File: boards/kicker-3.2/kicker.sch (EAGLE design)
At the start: 155 parts, among them J1 B2PS-VH(LF)(SN), J2 HFW8R-1ST, J3 B2PS-VH(LF)(SN), J4 B2PS-VH(LF)(SN), J5 2-PIN_2MM-H, J6 3-PIN_2MM-H, J7 !BTN_KCK_PRE_EXT, J8 !BTN_CHP_PRE_EXT, J9 !BTN_CHG_PRE_EXT, Q1 ATP302ATPAK, Q10 BSS806NSOT-23-3, Q2 IRFS4227, Q3 BSS127, Q4 BSS127, Q5 BSS127, Q6 BSS127, Q7 AOD1N60, T1 DA203X-ALDA2034, U1 MPM3620GQV-P, U2 15V, U3 LT3751FE, U4 AT32ATQFP44, U5 IX4427N, U6 MAX6817, U7 MAX6817

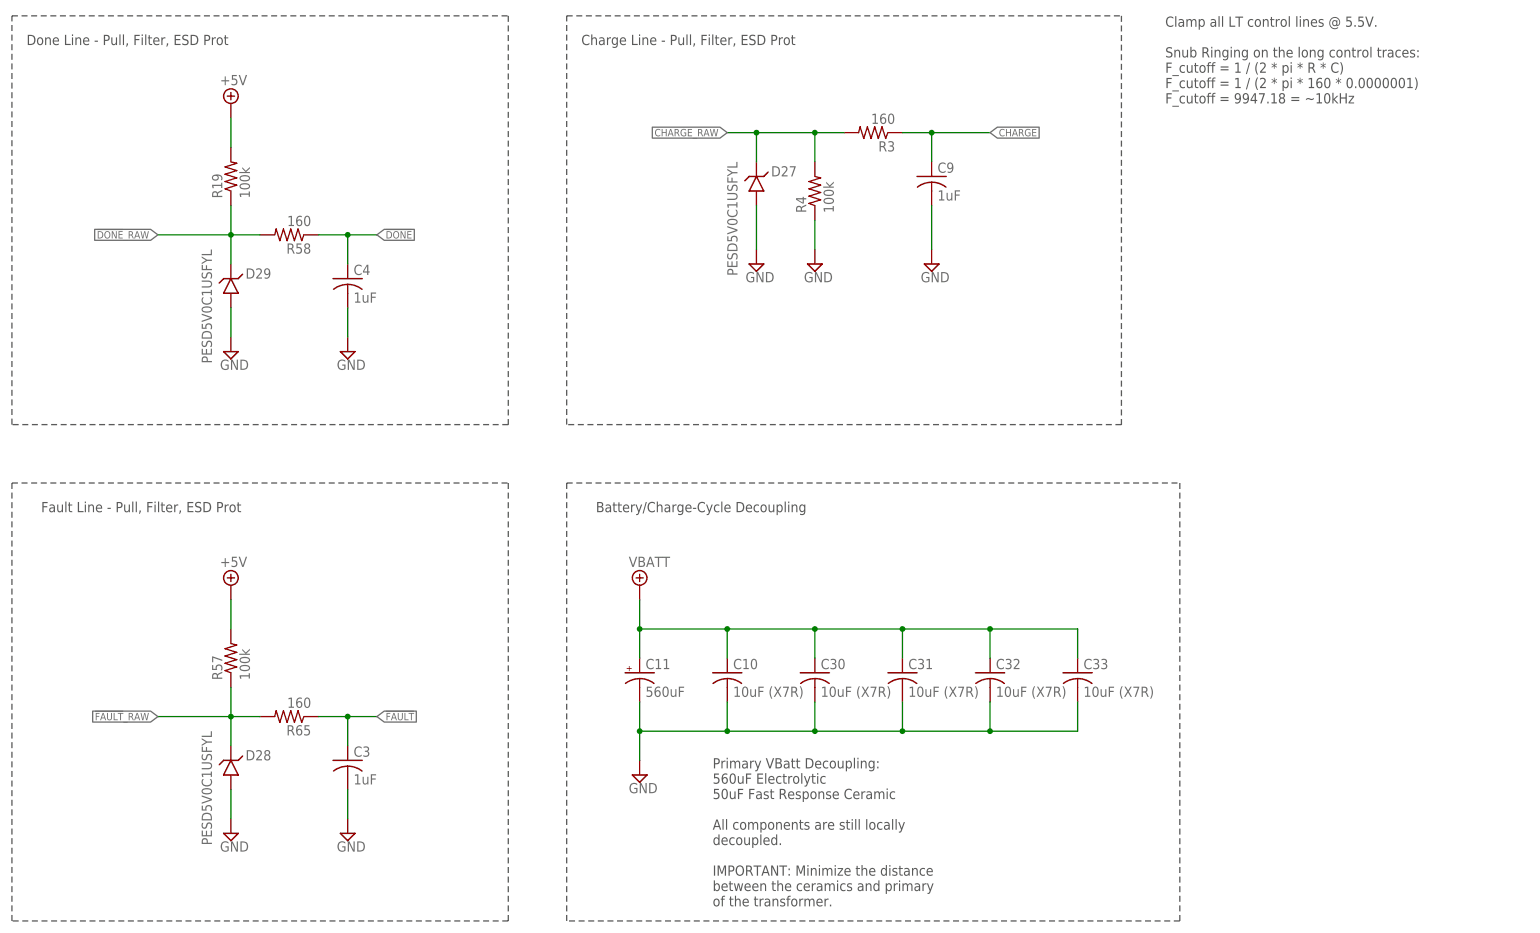
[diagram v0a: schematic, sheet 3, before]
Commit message: remove unnecessary TVS diodes clapming DIO rails
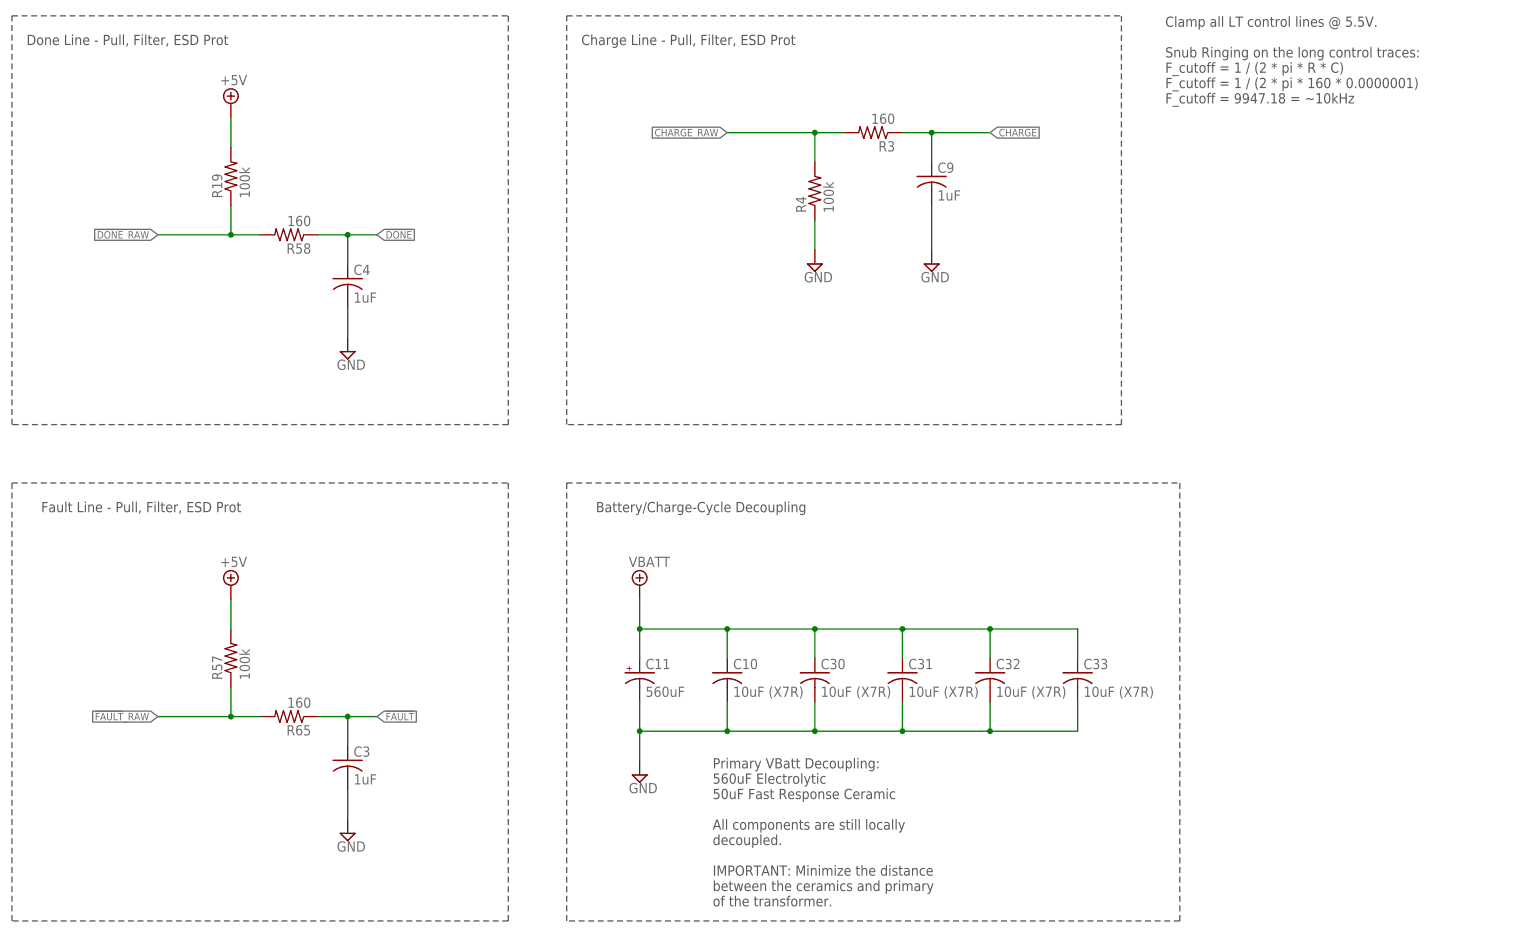
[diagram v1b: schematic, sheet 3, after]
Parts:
- removed D23, D27, D28, D29: PESD5V0C1USFYL, RoboJackets-Diodes:TVS0603
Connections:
- net !DONE!_RAW: no longer D29.C
- net !FAULT!_RAW: no longer D28.C
- net +5V: no longer D23.C
- net CHARGE_RAW: no longer D27.C
- net GND: no longer D23.A, D27.A, D28.A, D29.A
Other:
- note removed: "Clamp 5V @ 5.5V"
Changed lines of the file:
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@@
 <part name="R63" library="rcl" deviceset="R-US_" device="R1206" value="187k"/>
 <part name="R64" library="rcl" deviceset="R-US_" device="R0805" value="931"/>
-<part name="D23" library="RoboJackets-Diodes" deviceset="TVS" device="0603" package3d_urn="urn:adsk.eagle:package:23555/3" value="PESD5V0C1USFYL"/>
 <part name="D5" library="RoboJackets-LEDs" deviceset="LED-SMD" device="" technology="-YELLOW" value="YELLOW"/>
 <part name="D3" library="RoboJackets-LEDs" deviceset="LED-SMD" device="" technology="-BLUE" value="BLUE"/>
-<part name="SUPPLY98" library="supply2" deviceset="GND" device=""/>
 <part name="FRAME8" library="frames" library_urn="urn:adsk.eagle:library:229" deviceset="FRAME_A_L" device=""/>
 <part name="R19" library="rcl" deviceset="R-US_" device="R0603" value="100k"/>
@@
 <part name="R3" library="rcl" deviceset="R-US_" device="R0603" value="160"/>
 <part name="C9" library="rcl" deviceset="C-US" device="C0603" value="1uF"/>
-<part name="D27" library="RoboJackets-Diodes" deviceset="TVS" device="0603" package3d_urn="urn:adsk.eagle:package:23555/3" value="PESD5V0C1USFYL"/>
 <part name="SUPPLY12" library="supply2" deviceset="GND" device=""/>
-<part name="D28" library="RoboJackets-Diodes" deviceset="TVS" device="0603" package3d_urn="urn:adsk.eagle:package:23555/3" value="PESD5V0C1USFYL"/>
-<part name="D29" library="RoboJackets-Diodes" deviceset="TVS" device="0603" package3d_urn="urn:adsk.eagle:package:23555/3" value="PESD5V0C1USFYL"/>
 <part name="R4" library="rcl" deviceset="R-US_" device="R0603" value="100k"/>
 <part name="SUPPLY13" library="supply2" deviceset="GND" device=""/>
-<part name="SUPPLY100" library="supply2" deviceset="GND" device=""/>
-<part name="SUPPLY101" library="supply2" deviceset="GND" device=""/>
 <part name="SUPPLY102" library="supply2" deviceset="GND" device=""/>
 <part name="SUPPLY103" library="supply2" library_urn="urn:adsk.eagle:library:372" deviceset="+5V" device=""/>
 <part name="SUPPLY104" library="supply2" deviceset="GND" device=""/>
-<part name="SUPPLY105" library="supply2" deviceset="GND" device=""/>
 <part name="SUPPLY106" library="supply2" deviceset="GND" device=""/>
 <part name="C11" library="rcl" library_urn="urn:adsk.eagle:library:334" deviceset="CPOL-US" device="E7.5-18" package3d_urn="urn:adsk.eagle:package:23379/1" value="560uF"/>
@@
 <text x="101.6" y="147.32" size="1.778" layer="97">Clamp VBatt @ 22.2V</text>
 <text x="251.46" y="187.96" size="1.778" layer="97">&lt;50mA</text>
-<text x="137.16" y="78.74" size="1.778" layer="97">Clamp 5V @ 5.5V</text>
 <text x="17.78" y="53.34" size="1.778" layer="97">AAM R60 and Voltage Divider selected from datasheet</text>
 <text x="40.64" y="167.64" size="1.27" layer="97">Everything but the fuse holder
@@
 <attribute name="VALUE" x="114.935" y="70.485" size="1.778" layer="96"/>
 </instance>
-<instance part="D23" gate="G$1" x="132.08" y="86.36" smashed="yes">
-<attribute name="NAME" x="134.62" y="86.36" size="1.778" layer="95"/>
-<attribute name="VALUE" x="134.62" y="83.82" size="1.778" layer="96"/>
-</instance>
-<instance part="SUPPLY98" gate="GND" x="132.08" y="73.66" smashed="yes">
-<attribute name="VALUE" x="130.175" y="70.485" size="1.778" layer="96"/>
-</instance>
 <instance part="D24" gate="G$1" x="96.52" y="154.94" smashed="yes">
 <attribute name="NAME" x="99.06" y="154.94" size="1.778" layer="95"/>
@@
 <pinref part="SUPPLY96" gate="GND" pin="GND"/>
 <wire x1="116.84" y1="81.28" x2="116.84" y2="76.2" width="0.1524" layer="91"/>
-</segment>
-<segment>
-<pinref part="D23" gate="G$1" pin="A"/>
-<wire x1="132.08" y1="81.28" x2="132.08" y2="76.2" width="0.1524" layer="91"/>
-<pinref part="SUPPLY98" gate="GND" pin="GND"/>
 </segment>
 </net>
@@
 <wire x1="116.84" y1="91.44" x2="116.84" y2="88.9" width="0.1524" layer="91"/>
 <pinref part="SUPPLY3" gate="+5V" pin="+5V"/>
-<junction x="116.84" y="91.44"/>
-<pinref part="D23" gate="G$1" pin="C"/>
-<wire x1="116.84" y1="91.44" x2="132.08" y2="91.44" width="0.1524" layer="91"/>
-<wire x1="132.08" y1="91.44" x2="132.08" y2="88.9" width="0.1524" layer="91"/>
-<junction x="116.84" y="91.44"/>
 <pinref part="U1" gate="G$1" pin="OUT"/>
 <wire x1="88.9" y1="86.36" x2="99.06" y2="86.36" width="0.1524" layer="91"/>
@@
 <wire x1="104.14" y1="91.44" x2="116.84" y2="91.44" width="0.1524" layer="91"/>
 <junction x="104.14" y="91.44"/>
-<junction x="116.84" y="91.44"/>
 <wire x1="104.14" y1="101.6" x2="104.14" y2="91.44" width="0.1524" layer="91"/>
 </segment>
@@
 <attribute name="VALUE" x="176.276" y="168.529" size="1.778" layer="96"/>
 </instance>
-<instance part="D27" gate="G$1" x="144.78" y="172.72" smashed="yes">
-<attribute name="NAME" x="147.32" y="172.72" size="1.778" layer="95"/>
-<attribute name="VALUE" x="139.7" y="175.26" size="1.778" layer="96" rot="R270"/>
-</instance>
 <instance part="SUPPLY12" gate="GND" x="175.26" y="157.48" smashed="yes">
 <attribute name="VALUE" x="173.355" y="154.305" size="1.778" layer="96"/>
-</instance>
-<instance part="D28" gate="G$1" x="53.34" y="71.12" smashed="yes">
-<attribute name="NAME" x="55.88" y="71.12" size="1.778" layer="95"/>
-<attribute name="VALUE" x="48.26" y="76.2" size="1.778" layer="96" rot="R270"/>
-</instance>
-<instance part="D29" gate="G$1" x="53.34" y="154.94" smashed="yes">
-<attribute name="NAME" x="55.88" y="154.94" size="1.778" layer="95"/>
-<attribute name="VALUE" x="48.26" y="160.02" size="1.778" layer="96" rot="R270"/>
 </instance>
 <instance part="R4" gate="G$1" x="154.94" y="170.18" smashed="yes" rot="R90">
@@
 <attribute name="VALUE" x="153.035" y="154.305" size="1.778" layer="96"/>
 </instance>
-<instance part="SUPPLY100" gate="GND" x="144.78" y="157.48" smashed="yes">
-<attribute name="VALUE" x="142.875" y="154.305" size="1.778" layer="96"/>
-</instance>
-<instance part="SUPPLY101" gate="GND" x="53.34" y="58.42" smashed="yes">
-<attribute name="VALUE" x="51.435" y="55.245" size="1.778" layer="96"/>
-</instance>
 <instance part="SUPPLY102" gate="GND" x="73.66" y="58.42" smashed="yes">
 <attribute name="VALUE" x="71.755" y="55.245" size="1.778" layer="96"/>
@@
 <instance part="SUPPLY104" gate="GND" x="73.66" y="142.24" smashed="yes">
 <attribute name="VALUE" x="71.755" y="139.065" size="1.778" layer="96"/>
-</instance>
-<instance part="SUPPLY105" gate="GND" x="53.34" y="142.24" smashed="yes">
-<attribute name="VALUE" x="51.435" y="139.065" size="1.778" layer="96"/>
 </instance>
 <instance part="SUPPLY106" gate="GND" x="124.46" y="68.58" smashed="yes">
@@
 <label x="139.7" y="180.34" size="1.27" layer="95" rot="R180" xref="yes"/>
 <pinref part="R4" gate="G$1" pin="2"/>
-<wire x1="154.94" y1="180.34" x2="144.78" y2="180.34" width="0.1524" layer="91"/>
-<wire x1="144.78" y1="180.34" x2="139.7" y2="180.34" width="0.1524" layer="91"/>
+<wire x1="154.94" y1="180.34" x2="139.7" y2="180.34" width="0.1524" layer="91"/>
 <wire x1="154.94" y1="175.26" x2="154.94" y2="180.34" width="0.1524" layer="91"/>
 <junction x="154.94" y="180.34"/>
-<pinref part="D27" gate="G$1" pin="C"/>
-<wire x1="144.78" y1="175.26" x2="144.78" y2="180.34" width="0.1524" layer="91"/>
-<junction x="144.78" y="180.34"/>
 </segment>
 </net>
@@
 </segment>
 <segment>
-<pinref part="D27" gate="G$1" pin="A"/>
-<wire x1="144.78" y1="167.64" x2="144.78" y2="160.02" width="0.1524" layer="91"/>
-<pinref part="SUPPLY100" gate="GND" pin="GND"/>
-</segment>
-<segment>
-<pinref part="D28" gate="G$1" pin="A"/>
-<wire x1="53.34" y1="66.04" x2="53.34" y2="60.96" width="0.1524" layer="91"/>
-<pinref part="SUPPLY101" gate="GND" pin="GND"/>
-</segment>
-<segment>
 <pinref part="C3" gate="G$1" pin="2"/>
 <wire x1="73.66" y1="66.04" x2="73.66" y2="60.96" width="0.1524" layer="91"/>
@@
 <wire x1="73.66" y1="149.86" x2="73.66" y2="144.78" width="0.1524" layer="91"/>
 <pinref part="SUPPLY104" gate="GND" pin="GND"/>
-</segment>
-<segment>
-<pinref part="D29" gate="G$1" pin="A"/>
-<wire x1="53.34" y1="149.86" x2="53.34" y2="144.78" width="0.1524" layer="91"/>
-<pinref part="SUPPLY105" gate="GND" pin="GND"/>
 </segment>
 <segment>
@@
 <pinref part="R65" gate="G$1" pin="2"/>
 <label x="40.64" y="78.74" size="1.27" layer="97" rot="R180" xref="yes"/>
-<pinref part="D28" gate="G$1" pin="C"/>
 <wire x1="53.34" y1="78.74" x2="58.42" y2="78.74" width="0.1524" layer="91"/>
-<wire x1="53.34" y1="73.66" x2="53.34" y2="78.74" width="0.1524" layer="91"/>
 <junction x="53.34" y="78.74"/>
 <pinref part="R57" gate="G$1" pin="1"/>
@@
 <pinref part="R58" gate="G$1" pin="2"/>
 <wire x1="53.34" y1="162.56" x2="58.42" y2="162.56" width="0.1524" layer="91"/>
-<pinref part="D29" gate="G$1" pin="C"/>
-<wire x1="53.34" y1="157.48" x2="53.34" y2="162.56" width="0.1524" layer="91"/>
 <junction x="53.34" y="162.56"/>
 <wire x1="53.34" y1="162.56" x2="40.64" y2="162.56" width="0.1524" layer="91"/>
